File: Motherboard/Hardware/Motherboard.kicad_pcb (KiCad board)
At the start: 2 copper layers, 80 x 80 mm, 131 parts, among them J1 2411_06, J2 KLBR_4, Q1 BCX51, Q10 BC848, Q11 BC848, Q12 BC858, Q13 BC858, Q14 BC858, Q15 BC858, Q16 BC858, Q17 BC858, Q18 BC848, Q19 BC848, Q2 BC848, Q20 BC848, Q21 BC848, Q22 BC848, Q23 BC848, Q24 BC848, Q25 BC848, Q26 BC848, Q27 BC848, Q28 BC848, Q29 BC848, Q3 BC848, Q30 BC858, Q31 BC848, Q32 BC858, Q33 BC858, Q34 BC858, Q35 BC858, Q36 BC858, Q37 BC848, Q38 BC848, Q39 BC848, Q4 BC848, Q40 BC848, Q41 BC848, Q42 BC848, Q43 BC848, Q44 BC848, Q45 BC858, Q46 BC858, Q47 BC848, Q48 BC848, Q49 BC848, Q5 BC848, Q6 BC848, Q7 BCX51, Q8 BC848, Q9 BC848

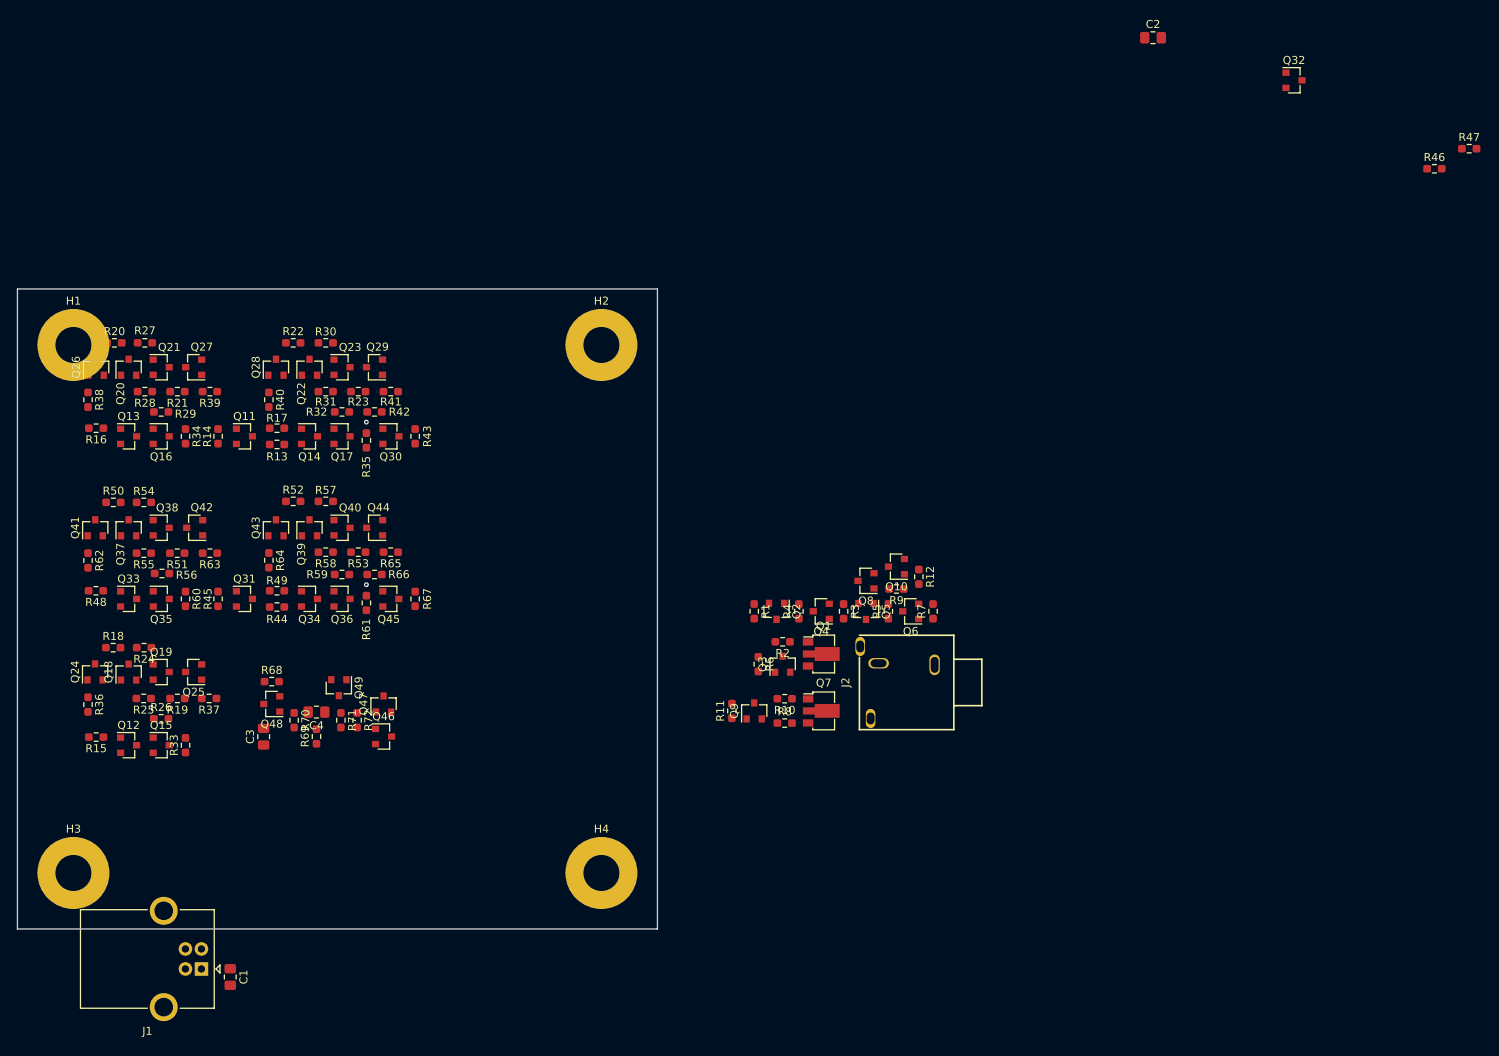
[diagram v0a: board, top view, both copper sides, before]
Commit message: Placed all components and mounting holes on PCB.
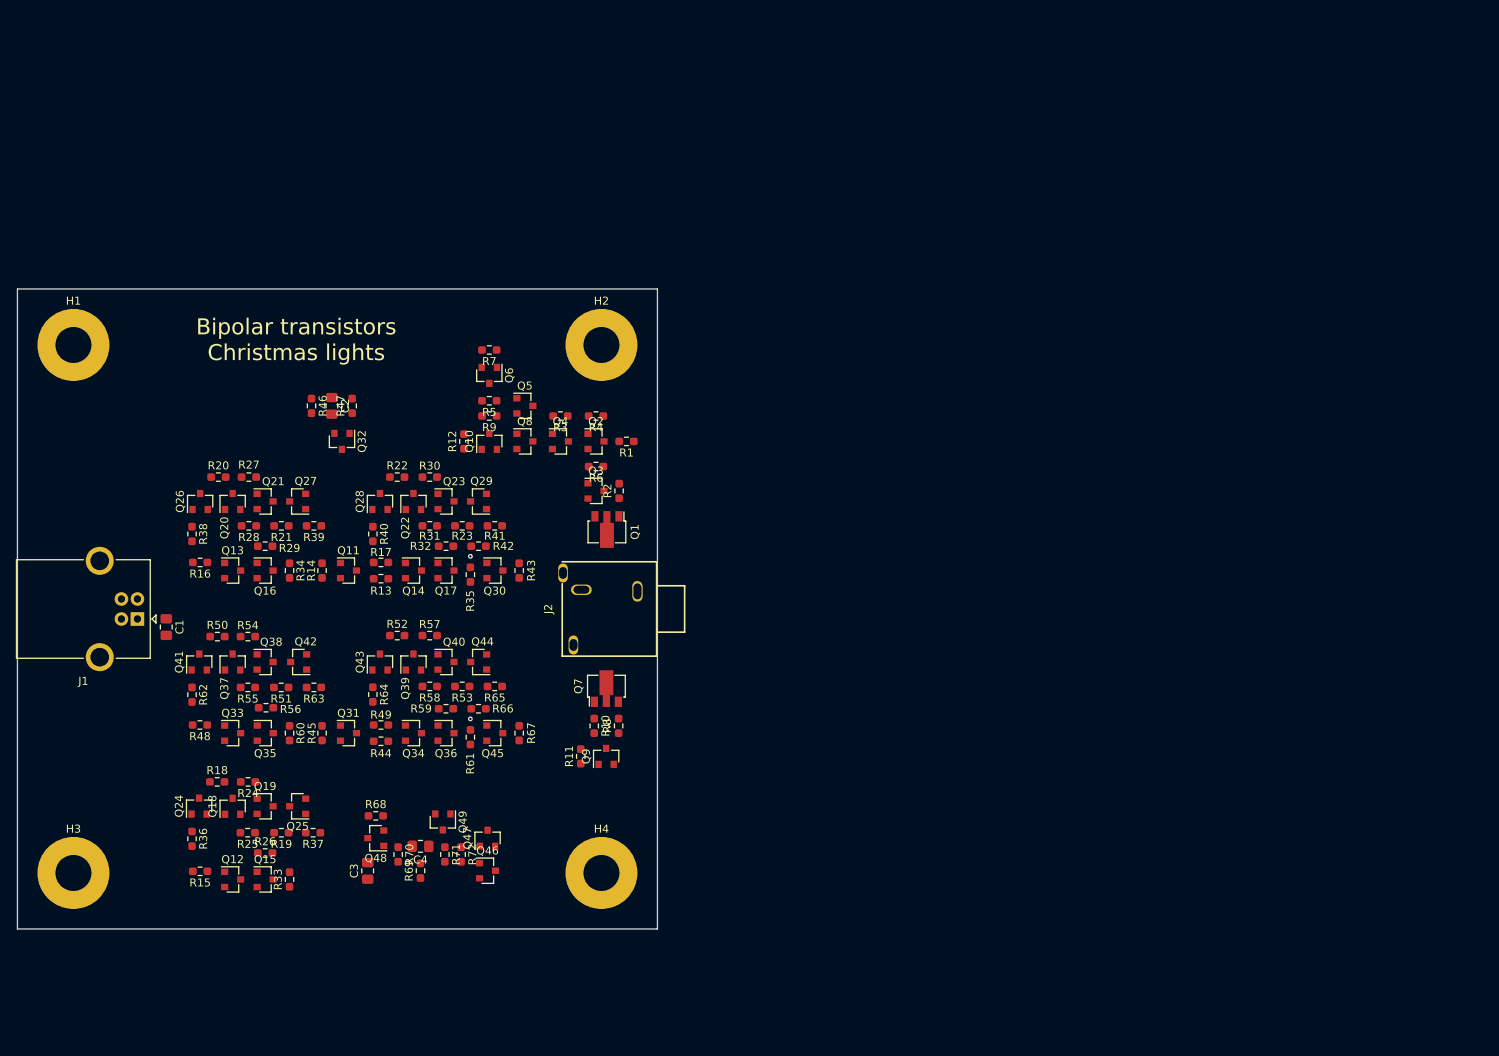
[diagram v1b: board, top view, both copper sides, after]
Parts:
- moved R46 143.5 mm to (111.8, 54.6), turned to 270 degrees
- moved R47 143.3 mm to (116.8, 54.6), turned to 90 degrees
- moved Q32 127.3 mm to (115.6, 59.1), turned to 270 degrees
- moved C2 112.5 mm to (114.3, 54.6), turned to 270 degrees
- moved R7 64.4 mm to (134.0, 47.6), turned to 180 degrees
- moved Q6 60.4 mm to (134.0, 50.8), turned to 270 degrees
- moved R12 59.3 mm to (130.8, 59.1), turned to 90 degrees
- moved R5 56.4 mm to (134.0, 54.0), turned to 180 degrees
- moved R9 55.3 mm to (134.0, 55.9)
- moved Q10 53.2 mm to (134.0, 59.1), turned to 90 degrees
- moved Q5 49.8 mm to (138.4, 54.6), turned to 0 degrees
- moved Q8 46.1 mm to (138.4, 59.1), turned to 0 degrees
- moved C1 44.5 mm to (93.6, 82.3)
- moved J1 44.5 mm to (90.0, 81.3)
- moved R3 43.0 mm to (142.9, 55.9), turned to 180 degrees
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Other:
- board text added: "22/02/2022"
- board text added: "Bipolar transistors Christmas lights"

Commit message: Routed PCB.
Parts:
- moved R12 12.4 mm to (141.5, 65.3), turned to 270 degrees
- moved R6 4.90 mm to (143.5, 65.3), turned to 90 degrees
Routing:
- net +5V: track 0.00 -> 412.4 mm, vias 0 -> 24
- net /Clock/CLK: track 0.00 -> 169.8 mm
- net /Ring_Counter/RESET: track 0.00 -> 130.4 mm, vias 0 -> 5
- net /Led_Control/COUNTER_BIT_0: track 0.00 -> 64.5 mm
- net /Ring_Counter/LATCH_2_OUT: track 0.00 -> 56.0 mm, vias 0 -> 4
- net /Ring_Counter/LATCH_1_OUT: track 0.00 -> 44.1 mm, vias 0 -> 2
- net /Led_Control/COUNTER_BIT_1: track 0.00 -> 36.4 mm, vias 0 -> 2
- net Net-(C3-Pad1): track 0.00 -> 18.9 mm, vias 0 -> 2
- net Net-(Q16-Pad3): track 0.00 -> 16.5 mm
- net Net-(Q35-Pad3): track 0.00 -> 16.2 mm
- net Net-(Q10-Pad1): track 0.00 -> 11.4 mm
- net Net-(Q40-Pad3): track 0.00 -> 10.5 mm
- net Net-(Q23-Pad3): track 0.00 -> 10.2 mm
- net Net-(Q2-Pad3): track 0.00 -> 9.71 mm
- net /Led_Control/LED_0: track 0.00 -> 9.26 mm
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- added copper zone on B.Cu, net GND
- added copper zone on F.Cu, net GND

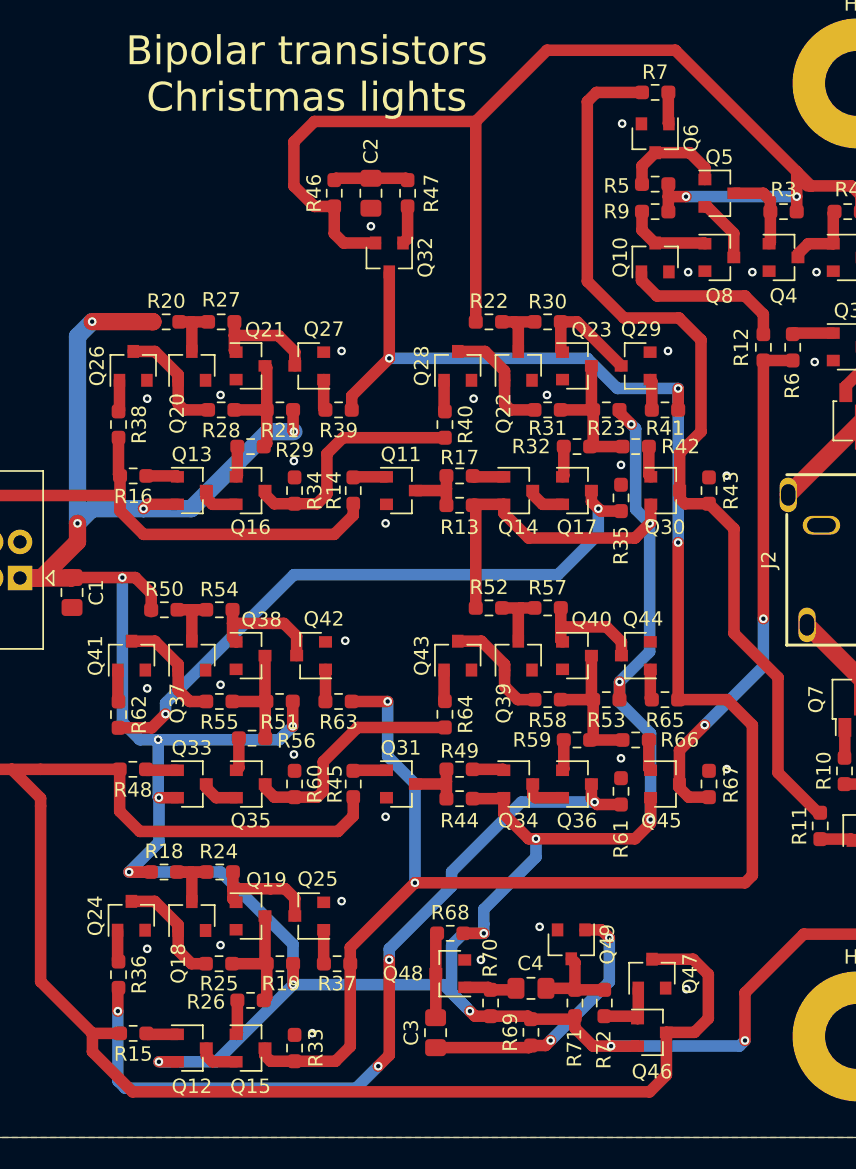
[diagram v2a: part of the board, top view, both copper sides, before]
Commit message: Disabled the motherboard clock circuit power supply while power-on reset delay is running to avoid clocking the RS gates while they are being reset by the power-on reset.
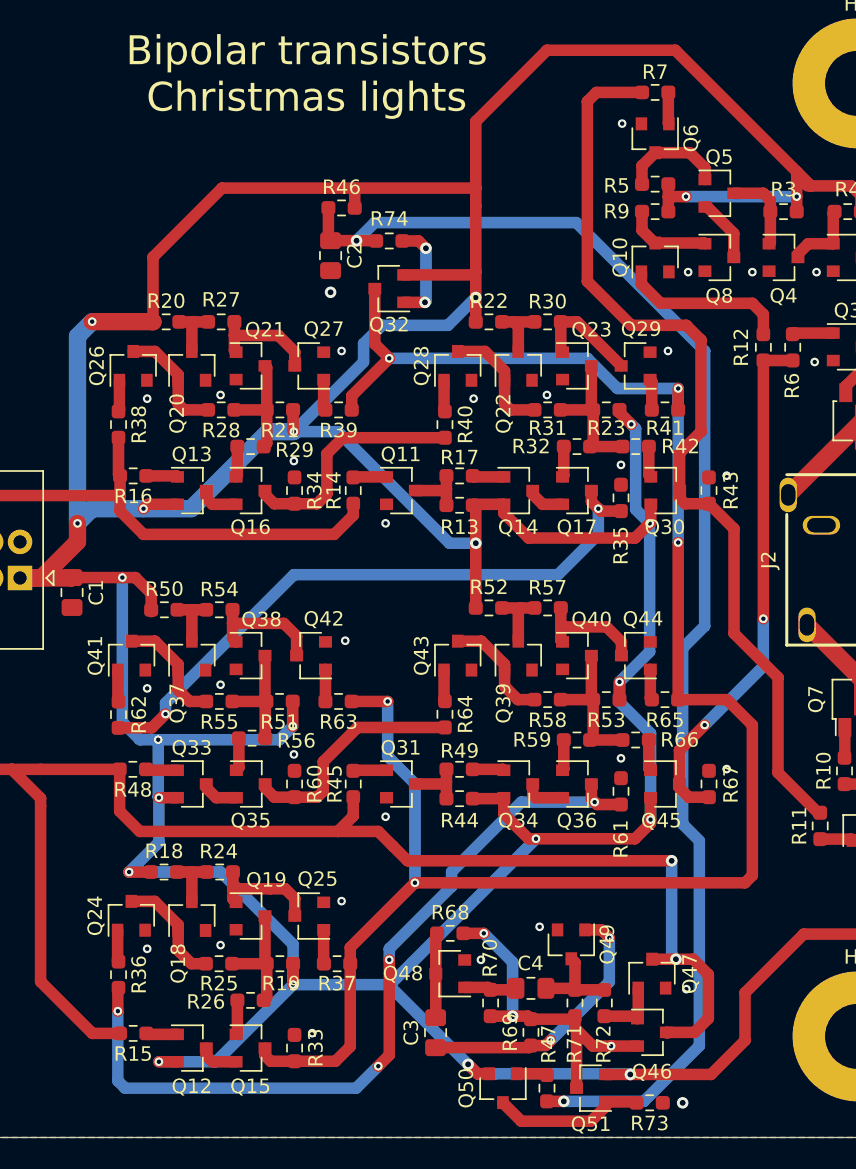
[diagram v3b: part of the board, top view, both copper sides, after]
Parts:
- added Q50: BC858, Package_TO_SOT_SMD:SOT-23, F.Cu at (123.4, 116.6)
- added Q51: BC858, Package_TO_SOT_SMD:SOT-23, F.Cu at (129.5, 116.6)
- added R73: 1K, Resistor_SMD:R_0603_1608Metric_Pad0.98x0.95mm_HandSolder, F.Cu at (133.6, 117.6)
- added R74: 1K, Resistor_SMD:R_0603_1608Metric_Pad0.98x0.95mm_HandSolder, F.Cu at (115.6, 57.9)
- moved R47 62.7 mm to (126.5, 116.6), turned to 270 degrees
- moved C2 5.14 mm to (111.5, 58.9)
- moved Q32 2.16 mm to (115.6, 61.2), turned to 180 degrees
- moved R46 1.14 mm to (112.3, 55.6), turned to 0 degrees
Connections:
- net Net-(C2-Pad1) renamed /Clock/POR
- Q46 pad 2: +5V -> Net-(Q46-Pad2)
- R47 pad 1: Net-(Q32-Pad1) -> Net-(Q50-Pad1)
- R68 pad 2: +5V -> Net-(Q46-Pad2)
- R69 pad 2: +5V -> Net-(Q46-Pad2)
- R70 pad 2: +5V -> Net-(Q46-Pad2)
- R71 pad 2: +5V -> Net-(Q46-Pad2)
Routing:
- net /Clock/POR: track 5.18 -> 95.2 mm, vias 0 -> 2
- net +5V: track 412.4 -> 459.6 mm
- net Net-(Q46-Pad2): track 0.00 -> 23.9 mm, vias 0 -> 3
- net /Clock/CLK: track 169.8 -> 155.1 mm, vias 0 -> 2
- net Net-(Q50-Pad3): track 0.00 -> 10.6 mm
- net Net-(Q32-Pad1): track 2.67 -> 7.08 mm, vias 0 -> 2
- net Net-(Q50-Pad1): track 0.00 -> 2.13 mm
- net /Ring_Counter/RESET: track 130.4 -> 129.7 mm
- net GND: vias 31 -> 32

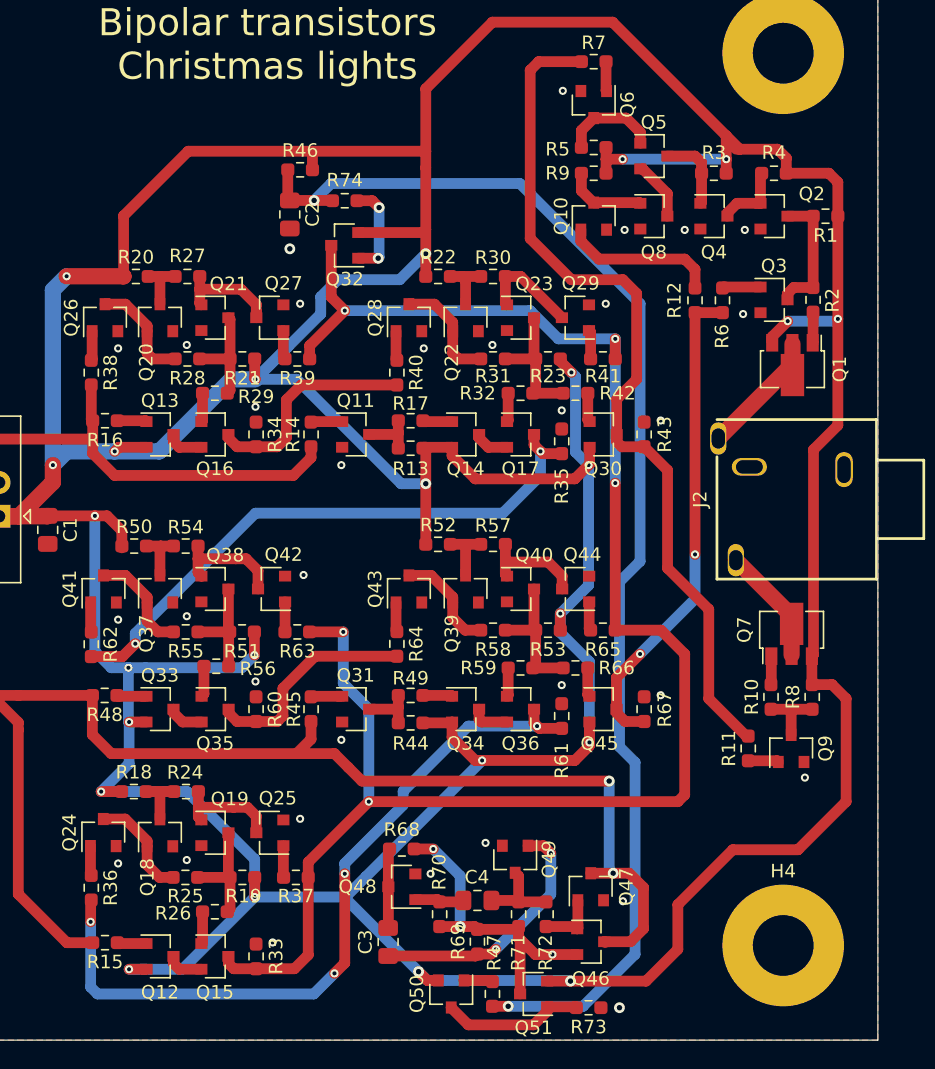
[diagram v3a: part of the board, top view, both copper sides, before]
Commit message: Updated the motherboard PCB to KiCad 7.
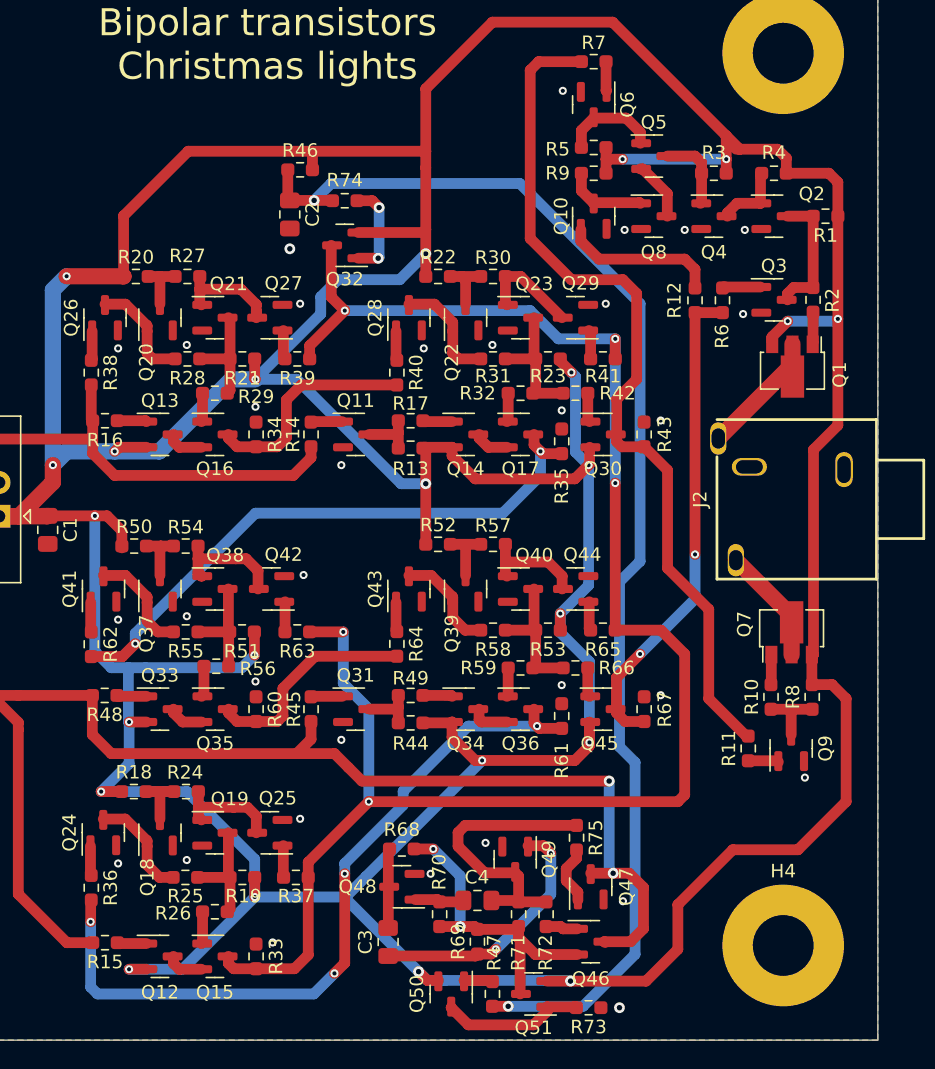
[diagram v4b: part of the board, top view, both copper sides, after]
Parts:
- added R75: 10K, Resistor_SMD:R_0603_1608Metric_Pad0.98x0.95mm_HandSolder, F.Cu at (132.7, 105.0)
- R72: value 1K -> 10K
- moved Q1 0.42 mm to (148.7, 70.5)
- moved Q7 0.42 mm to (148.6, 89.5)
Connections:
- J1 pad 2: Net-(J1-Pad2) -> unconnected-(J1-D--Pad2)
- J1 pad 3: Net-(J1-Pad3) -> unconnected-(J1-D+-Pad3)
- Q46 pad 1: Net-(Q46-Pad1) -> Net-(Q46-B)
- Q47 pad 1: Net-(Q46-Pad1) -> Net-(Q47-B)
- R72 pad 2: Net-(Q46-Pad1) -> Net-(Q46-B)
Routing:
- net Net-(Q49-C): track 6.34 -> 21.4 mm
- net Net-(Q46-Pad1): track 4.51 -> 0.00 mm
- net Net-(Q47-B): track 0.00 -> 4.39 mm
- net +5V: track 459.6 -> 456.2 mm, vias 24 -> 23
- net Net-(Q46-B): track 0.00 -> 2.37 mm
- net Net-(Q46-E): vias 3 -> 2
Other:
- net class Default removed
